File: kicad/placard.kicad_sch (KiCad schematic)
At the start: 0 parts

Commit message: KiCad schematic: 11 main-board sheets and the cartridge, generated
src/scripts/gen_kicad_schematic.py (with kicad_sch_lib.py) writes the
sheets from docs/SCHEMATIC_PLAN.md with every pin's net listed from the
PLD pin lists, basys_top.vhd and the docs.  Decoupling Cn beside each Un,
global labels between sheets, staggered 2 mm labels.  --check compares
KiCad's exported netlist with the script (260 main-board nets, 35 on the
cartridge, no differences).  PDFs in schematics/.  IO.md SD divider refs
now R1003-R1008.

Co-Authored-By: Claude Opus 5.5 (1M context) <noreply@anthropic.com>
Claude-Session: https://claude.ai/code/session_01L9AkLuEg13EebxDmgXsaEp
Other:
- added sheet ALU and registers (alu_regs.kicad_sch)
- added sheet Control (control.kicad_sch)
- added sheet Data bus (data_bus.kicad_sch)
- added sheet Expansion slots (expansion.kicad_sch)
- added sheet Memory and I/O decode (memory.kicad_sch)
- added sheet Power and clock (power.kicad_sch)
- added sheet Program counter and address mux (pc_mux.kicad_sch)
- added sheet Shared port (shared_port.kicad_sch)
- added sheet Video and audio out (video_out.kicad_sch)
- added sheet Video timing (video_timing.kicad_sch)
- note added: "35 chips + U40 regulator (docs/CHIPS.md numbers; U24, U28, U30, U33, U34 are not used)."
- note added: "Decoupling: every chip's 100 nF Cn sits beside Un on its own sheet."
- note added: "HOLD / RUN jumpers"
- note added: "Hierarchy: each box is one sheet; the sheets connect through global labels"
- note added: "J13 USB-C, F201, U40 3.3 V"
- note added: "J9-J12 card-edge slots"
- note added: "Placard main board"
- note added: "Power: +5V, GND, +3V3 (SD card), GNDA (audio, joined to GND on sheet 2)."
- note added: "R601-R608, RN601"
- note added: "The ROM cartridge is its own project: kicad/cartridge/."
- note added: "U1 State, U2 Branch"
- note added: "U11 memory control"
- note added: "U12 I/O decode, U25 map"
- note added: "U13 H, U14 V counters"
- note added: "U15 Sync, U35 audio slots"
- note added: "U16 color decoder, VGA"
- note added: "U17 instruction register"
- note added: "U18 D register"
- note added: "U19 AC, U20 X, U21 Y"
- note added: "U22 pixel buffer, U23 line code"
- note added: "U26, U27 source drivers"
- note added: "U29 line read"
- note added: "U3, U4 program counter"
- note added: "U31, U32 RAM, J8 cartridge"
- note added: "U36 audio DAC, J6"
- note added: "U37 latch, U38 port PLD"
- note added: "U39 rows, J1-J5"
- note added: "U5, U6 ALU"
- note added: "U7-U10 address mux"
- note added: "X1 25.175 MHz, U41 clock gate"
- company: (none) -> Placard computer
- title: Placard -> Placard: Main board
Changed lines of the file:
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@@
 (kicad_sch (version 20230121) (generator eeschema)
   (paper "A3")
-  (title_block
-    (title "Placard")
-    (date "2026-10-19")
-    (rev "0")
-    (comment 1 "PLD computer: see docs/CHIPS.md for parts and U-numbers")
-  )
-  (sheet_instances
-    (path "/" (page "1"))
-  )
+  (title_block (title "Placard: Main board") (date "2026-10-20") (rev "1") (company "Placard computer") (comment 1 "Generated by src/scripts/gen_kicad_schematic.py; plan in docs/SCHEMATIC_PLAN.md") (comment 2 "Chip numbers U1-U41 = docs/CHIPS.md; decoupling Cn goes with Un"))
+  (text "Placard main board" (at 15 22 0) (effects (font (size 6 6) bold) (justify left bottom)))
+  (text "Hierarchy: each box is one sheet; the sheets connect through global labels" (at 15 30 0) (effects (font (size 3 3)) (justify left bottom)))
+  (text "J13 USB-C, F201, U40 3.3 V" (at 23 60 0) (effects (font (size 2.5 2.5)) (justify left bottom)))
+  (text "X1 25.175 MHz, U41 clock gate" (at 23 67 0) (effects (font (size 2.5 2.5)) (justify left bottom)))
+  (text "HOLD / RUN jumpers" (at 23 74 0) (effects (font (size 2.5 2.5)) (justify left bottom)))
+  (text "U1 State, U2 Branch" (at 118 60 0) (effects (font (size 2.5 2.5)) (justify left bottom)))
+  (text "U17 instruction register" (at 118 67 0) (effects (font (size 2.5 2.5)) (justify left bottom)))
+  (text "U3, U4 program counter" (at 213 60 0) (effects (font (size 2.5 2.5)) (justify left bottom)))
+  (text "U7-U10 address mux" (at 213 67 0) (effects (font (size 2.5 2.5)) (justify left bottom)))
+  (text "U31, U32 RAM, J8 cartridge" (at 308 60 0) (effects (font (size 2.5 2.5)) (justify left bottom)))
+  (text "U11 memory control" (at 308 67 0) (effects (font (size 2.5 2.5)) (justify left bottom)))
+  (text "U12 I/O decode, U25 map" (at 308 74 0) (effects (font (size 2.5 2.5)) (justify left bottom)))
+  (text "U5, U6 ALU" (at 118 115 0) (effects (font (size 2.5 2.5)) (justify left bottom)))
+  (text "U19 AC, U20 X, U21 Y" (at 118 122 0) (effects (font (size 2.5 2.5)) (justify left bottom)))
+  (text "U18 D register" (at 213 115 0) (effects (font (size 2.5 2.5)) (justify left bottom)))
+  (text "U26, U27 source drivers" (at 213 122 0) (effects (font (size 2.5 2.5)) (justify left bottom)))
+  (text "R601-R608, RN601" (at 213 129 0) (effects (font (size 2.5 2.5)) (justify left bottom)))
+  (text "U13 H, U14 V counters" (at 23 115 0) (effects (font (size 2.5 2.5)) (justify left bottom)))
+  (text "U15 Sync, U35 audio slots" (at 23 122 0) (effects (font (size 2.5 2.5)) (justify left bottom)))
+  (text "U29 line read" (at 23 129 0) (effects (font (size 2.5 2.5)) (justify left bottom)))
+  (text "U22 pixel buffer, U23 line code" (at 23 170 0) (effects (font (size 2.5 2.5)) (justify left bottom)))
+  (text "U16 color decoder, VGA" (at 23 177 0) (effects (font (size 2.5 2.5)) (justify left bottom)))
+  (text "U36 audio DAC, J6" (at 23 184 0) (effects (font (size 2.5 2.5)) (justify left bottom)))
+  (text "U37 latch, U38 port PLD" (at 118 170 0) (effects (font (size 2.5 2.5)) (justify left bottom)))
+  (text "U39 rows, J1-J5" (at 118 177 0) (effects (font (size 2.5 2.5)) (justify left bottom)))
+  (text "J9-J12 card-edge slots" (at 308 115 0) (effects (font (size 2.5 2.5)) (justify left bottom)))
+  (text "35 chips + U40 regulator (docs/CHIPS.md numbers; U24, U28, U30, U33, U34 are not used)." (at 20 220 0) (effects (font (size 3 3)) (justify left bottom)))
+  (text "Decoupling: every chip's 100 nF Cn sits beside Un on its own sheet." (at 20 224.8 0) (effects (font (size 3 3)) (justify left bottom)))
+  (text "Power: +5V, GND, +3V3 (SD card), GNDA (audio, joined to GND on sheet 2)." (at 20 229.6 0) (effects (font (size 3 3)) (justify left bottom)))
+  (text "The ROM cartridge is its own project: kicad/cartridge/." (at 20 234.4 0) (effects (font (size 3 3)) (justify left bottom)))
+  (sheet (at 20 50) (size 80 35) (fields_autoplaced) (stroke (width 0.3) (type solid)) (fill (color 255 255 225 1.0000)) (property "Sheetname" "Power and clock" (at 20 49.2 0) (effects (font (size 3 3) bold) (justify left bottom))) (property "Sheetfile" "power.kicad_sch" (at 20 85.8 0) (effects (font (size 2 2)) (justify left top))) (instances (project "placard" (path "/e3450542-4ffc-59d4-a4a7-45636233928a" (page "2")))))
+  (sheet (at 115 50) (size 80 35) (fields_autoplaced) (stroke (width 0.3) (type solid)) (fill (color 255 255 225 1.0000)) (property "Sheetname" "Control" (at 115 49.2 0) (effects (font (size 3 3) bold) (justify left bottom))) (property "Sheetfile" "control.kicad_sch" (at 115 85.8 0) (effects (font (size 2 2)) (justify left top))) (instances (project "placard" (path "/e3450542-4ffc-59d4-a4a7-45636233928a" (page "3")))))
+  (sheet (at 210 50) (size 80 35) (fields_autoplaced) (stroke (width 0.3) (type solid)) (fill (color 255 255 225 1.0000)) (property "Sheetname" "Program counter and address mux" (at 210 49.2 0) (effects (font (size 3 3) bold) (justify left bottom))) (property "Sheetfile" "pc_mux.kicad_sch" (at 210 85.8 0) (effects (font (size 2 2)) (justify left top))) (instances (project "placard" (path "/e3450542-4ffc-59d4-a4a7-45636233928a" (page "4")))))
+  (sheet (at 305 50) (size 95 35) (fields_autoplaced) (stroke (width 0.3) (type solid)) (fill (color 255 255 225 1.0000)) (property "Sheetname" "Memory and I/O decode" (at 305 49.2 0) (effects (font (size 3 3) bold) (justify left bottom))) (property "Sheetfile" "memory.kicad_sch" (at 305 85.8 0) (effects (font (size 2 2)) (justify left top))) (instances (project "placard" (path "/e3450542-4ffc-59d4-a4a7-45636233928a" (page "7")))))
+  (sheet (at 115 105) (size 80 35) (fields_autoplaced) (stroke (width 0.3) (type solid)) (fill (color 255 255 225 1.0000)) (property "Sheetname" "ALU and registers" (at 115 104.2 0) (effects (font (size 3 3) bold) (justify left bottom))) (property "Sheetfile" "alu_regs.kicad_sch" (at 115 140.8 0) (effects (font (size 2 2)) (justify left top))) (instances (project "placard" (path "/e3450542-4ffc-59d4-a4a7-45636233928a" (page "5")))))
+  (sheet (at 210 105) (size 80 35) (fields_autoplaced) (stroke (width 0.3) (type solid)) (fill (color 255 255 225 1.0000)) (property "Sheetname" "Data bus" (at 210 104.2 0) (effects (font (size 3 3) bold) (justify left bottom))) (property "Sheetfile" "data_bus.kicad_sch" (at 210 140.8 0) (effects (font (size 2 2)) (justify left top))) (instances (project "placard" (path "/e3450542-4ffc-59d4-a4a7-45636233928a" (page "6")))))
+  (sheet (at 20 105) (size 80 35) (fields_autoplaced) (stroke (width 0.3) (type solid)) (fill (color 255 255 225 1.0000)) (property "Sheetname" "Video timing" (at 20 104.2 0) (effects (font (size 3 3) bold) (justify left bottom))) (property "Sheetfile" "video_timing.kicad_sch" (at 20 140.8 0) (effects (font (size 2 2)) (justify left top))) (instances (project "placard" (path "/e3450542-4ffc-59d4-a4a7-45636233928a" (page "8")))))
+  (sheet (at 20 160) (size 80 35) (fields_autoplaced) (stroke (width 0.3) (type solid)) (fill (color 255 255 225 1.0000)) (property "Sheetname" "Video and audio out" (at 20 159.2 0) (effects (font (size 3 3) bold) (justify left bottom))) (property "Sheetfile" "video_out.kicad_sch" (at 20 195.8 0) (effects (font (size 2 2)) (justify left top))) (instances (project "placard" (path "/e3450542-4ffc-59d4-a4a7-45636233928a" (page "9")))))
+  (sheet (at 115 160) (size 80 35) (fields_autoplaced) (stroke (width 0.3) (type solid)) (fill (color 255 255 225 1.0000)) (property "Sheetname" "Shared port" (at 115 159.2 0) (effects (font (size 3 3) bold) (justify left bottom))) (property "Sheetfile" "shared_port.kicad_sch" (at 115 195.8 0) (effects (font (size 2 2)) (justify left top))) (instances (project "placard" (path "/e3450542-4ffc-59d4-a4a7-45636233928a" (page "10")))))
+  (sheet (at 305 105) (size 95 35) (fields_autoplaced) (stroke (width 0.3) (type solid)) (fill (color 255 255 225 1.0000)) (property "Sheetname" "Expansion slots" (at 305 104.2 0) (effects (font (size 3 3) bold) (justify left bottom))) (property "Sheetfile" "expansion.kicad_sch" (at 305 140.8 0) (effects (font (size 2 2)) (justify left top))) (instances (project "placard" (path "/e3450542-4ffc-59d4-a4a7-45636233928a" (page "11")))))
+  (sheet_instances (path "/" (page "1")))
 )

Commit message: Cartridge loader everywhere: FPGA cartridge model, random RAM, nop at x0000
- src/hdl/cartridge.vhd: the ROM cartridge (loader PLD, EEPROMs from
  rom.mem, SRAM written by /SR_WE); basys_top uses it for RUN, STALL_OUT
  and the ROM data, and the IR PLD replaces the instruction F377
- main RAM and cartridge SRAM start random (gen_random_ram.tcl writes
  ram.mem and cart_ram.mem); build, fast and create_project scripts
  updated, new .vhd files are added to an existing project
- rom_boot and the bring-up ROM keep a nop at x0000 for the hand-off;
  menu and bring-up images rebuilt
- schematic: IR PLD as U17, no 74AC32, STALL_IN/STALL_OUT/PC_ENABLE on
  the cartridge connector, cartridge without the 541; PDFs regenerated
- docs: ROM, CHIPS, BRINGUP, EXPANSION, timing, PLD usage, kitting,
  schematic plan, block diagram
- src/sim/tb_top_load.vhd: whole FPGA model from power-up through the
  load and boot

Co-Authored-By: Claude Opus 5.5 (1M context) <noreply@anthropic.com>
Claude-Session: https://claude.ai/code/session_01PNJoPfzmo1tu8EorCrua96
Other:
- note added: "34 chips + U40 regulator (docs/CHIPS.md numbers; U24, U28, U30, U33, U34 are not used)."
- note added: "STALL / RUN jumpers"
- note added: "U17 instruction register PLD"
- note added: "X1 25.175 MHz clock"
- note removed: "35 chips + U40 regulator (docs/CHIPS.md numbers; U24, U28, U30, U33, U34 are not used)."
- note removed: "HOLD / RUN jumpers"
- note removed: "U17 instruction register"
- note removed: "X1 25.175 MHz, U41 clock gate"
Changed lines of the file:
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@@
   (text "Hierarchy: each box is one sheet; the sheets connect through global labels" (at 15 30 0) (effects (font (size 3 3)) (justify left bottom)))
   (text "J13 USB-C, F201, U40 3.3 V" (at 23 60 0) (effects (font (size 2.5 2.5)) (justify left bottom)))
-  (text "X1 25.175 MHz, U41 clock gate" (at 23 67 0) (effects (font (size 2.5 2.5)) (justify left bottom)))
-  (text "HOLD / RUN jumpers" (at 23 74 0) (effects (font (size 2.5 2.5)) (justify left bottom)))
+  (text "X1 25.175 MHz clock" (at 23 67 0) (effects (font (size 2.5 2.5)) (justify left bottom)))
+  (text "STALL / RUN jumpers" (at 23 74 0) (effects (font (size 2.5 2.5)) (justify left bottom)))
   (text "U1 State, U2 Branch" (at 118 60 0) (effects (font (size 2.5 2.5)) (justify left bottom)))
-  (text "U17 instruction register" (at 118 67 0) (effects (font (size 2.5 2.5)) (justify left bottom)))
+  (text "U17 instruction register PLD" (at 118 67 0) (effects (font (size 2.5 2.5)) (justify left bottom)))
   (text "U3, U4 program counter" (at 213 60 0) (effects (font (size 2.5 2.5)) (justify left bottom)))
   (text "U7-U10 address mux" (at 213 67 0) (effects (font (size 2.5 2.5)) (justify left bottom)))
@@
   (text "U39 rows, J1-J5" (at 118 177 0) (effects (font (size 2.5 2.5)) (justify left bottom)))
   (text "J9-J12 card-edge slots" (at 308 115 0) (effects (font (size 2.5 2.5)) (justify left bottom)))
-  (text "35 chips + U40 regulator (docs/CHIPS.md numbers; U24, U28, U30, U33, U34 are not used)." (at 20 220 0) (effects (font (size 3 3)) (justify left bottom)))
+  (text "34 chips + U40 regulator (docs/CHIPS.md numbers; U24, U28, U30, U33, U34 are not used)." (at 20 220 0) (effects (font (size 3 3)) (justify left bottom)))
   (text "Decoupling: every chip's 100 nF Cn sits beside Un on its own sheet." (at 20 224.8 0) (effects (font (size 3 3)) (justify left bottom)))
   (text "Power: +5V, GND, +3V3 (SD card), GNDA (audio, joined to GND on sheet 2)." (at 20 229.6 0) (effects (font (size 3 3)) (justify left bottom)))

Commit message: Number parts from 1 for each kind; US zigzag resistor symbols
Main board R1-R54, RN1-RN2, D1-D5, JP1-JP2, F1, NT1, non-decoupling
capacitors C41-C46 (decaps keep Cn = Un); keyboard keys 1-63 row by row
(SWn, Dn, Rn per key). Resistors use R_US / R_Network08_US. --check now
fails on gaps or hundreds in the numbering. PDFs regenerated.

Co-Authored-By: Claude Opus 5.5 (1M context) <noreply@anthropic.com>
Claude-Session: https://claude.ai/code/session_01L9AkLuEg13EebxDmgXsaEp
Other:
- note added: "J13 USB-C, F1, U40 3.3 V"
- note added: "R5-R12, RN1"
- note removed: "J13 USB-C, F201, U40 3.3 V"
- note removed: "R601-R608, RN601"
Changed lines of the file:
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@@
   (text "Placard main board" (at 15 22 0) (effects (font (size 6 6) bold) (justify left bottom)))
   (text "Hierarchy: each box is one sheet; the sheets connect through global labels" (at 15 30 0) (effects (font (size 3 3)) (justify left bottom)))
-  (text "J13 USB-C, F201, U40 3.3 V" (at 23 60 0) (effects (font (size 2.5 2.5)) (justify left bottom)))
+  (text "J13 USB-C, F1, U40 3.3 V" (at 23 60 0) (effects (font (size 2.5 2.5)) (justify left bottom)))
   (text "X1 25.175 MHz clock" (at 23 67 0) (effects (font (size 2.5 2.5)) (justify left bottom)))
   (text "STALL / RUN jumpers" (at 23 74 0) (effects (font (size 2.5 2.5)) (justify left bottom)))
@@
   (text "U18 D register" (at 213 115 0) (effects (font (size 2.5 2.5)) (justify left bottom)))
   (text "U26, U27 source drivers" (at 213 122 0) (effects (font (size 2.5 2.5)) (justify left bottom)))
-  (text "R601-R608, RN601" (at 213 129 0) (effects (font (size 2.5 2.5)) (justify left bottom)))
+  (text "R5-R12, RN1" (at 213 129 0) (effects (font (size 2.5 2.5)) (justify left bottom)))
   (text "U13 H, U14 V counters" (at 23 115 0) (effects (font (size 2.5 2.5)) (justify left bottom)))
   (text "U15 Sync, U35 audio slots" (at 23 122 0) (effects (font (size 2.5 2.5)) (justify left bottom)))

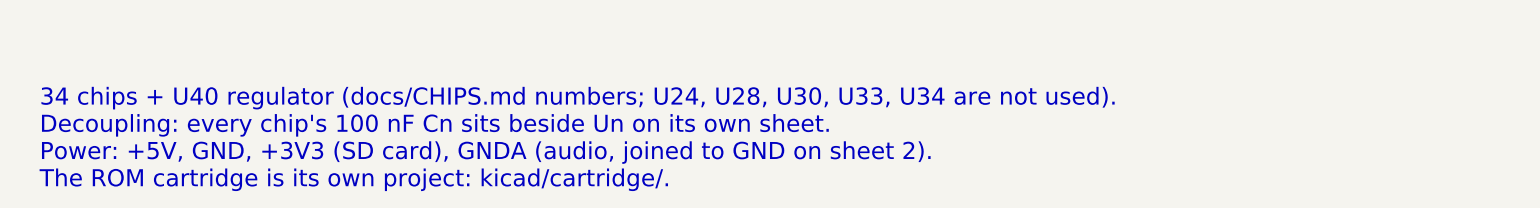
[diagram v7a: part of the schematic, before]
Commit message: Split the ROM cartridge into separate 32K and 64K boards
Two KiCad projects replace the one cartridge with the 32K/64K solder
jumper JP1: kicad/cartridge_64k (U1 loader PLD, U2/U3 EEPROMs, U4/U5
SRAMs) and kicad/cartridge_32k (U1, U2 EEPROM, U3 SRAM, /CE tied to
GND). Each has a placed, netted, unrouted 2-layer board from the new
gen_kicad_cart_pcb.py, with the M3 hole H1 in the gap right above U1 so
it is at the same place (19.5, 25.1 mm) on both boards. New footprint
Card_Edge_87715-9106 (A row on the parts side). Schematic PDFs, BOM and
docs updated; gen_cart_placement.py replaced by the board drawings.

Co-Authored-By: Claude Opus 5.5 (1M context) <noreply@anthropic.com>
Claude-Session: https://claude.ai/code/session_01V16uxpbjEWC9E2eDda9bhu
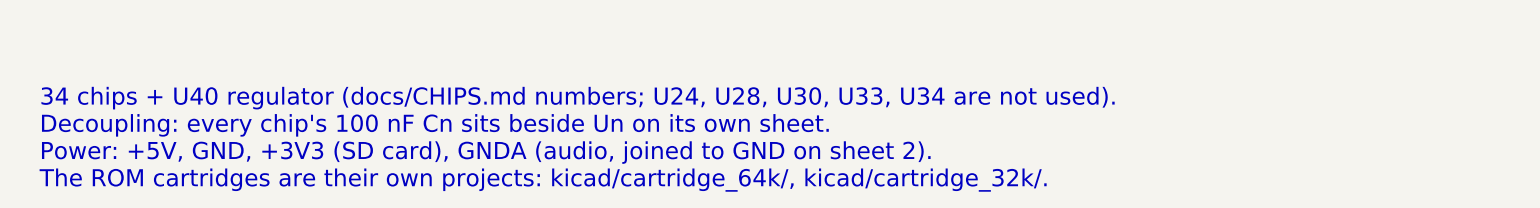
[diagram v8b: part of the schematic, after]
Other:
- note added: "The ROM cartridges are their own projects: kicad/cartridge_64k/, kicad/cartridge_32k/."
- note removed: "The ROM cartridge is its own project: kicad/cartridge/."
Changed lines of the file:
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@@
 (kicad_sch (version 20230121) (generator eeschema)
   (paper "A3")
-  (title_block (title "Placard: Main board") (date "2026-10-23") (rev "1") (company "Placard computer") (comment 1 "Generated by src/scripts/gen_kicad_schematic.py; plan in docs/SCHEMATIC_PLAN.md") (comment 2 "Chip numbers U1-U40 = docs/CHIPS.md; decoupling Cn goes with Un"))
+  (title_block (title "Placard: Main board") (date "2026-10-24") (rev "1") (company "Placard computer") (comment 1 "Generated by src/scripts/gen_kicad_schematic.py; plan in docs/SCHEMATIC_PLAN.md") (comment 2 "Chip numbers U1-U40 = docs/CHIPS.md; decoupling Cn goes with Un"))
   (text "Placard main board" (at 15 22 0) (effects (font (size 6 6) bold) (justify left bottom)))
   (text "Hierarchy: each box is one sheet; the sheets connect through global labels" (at 15 30 0) (effects (font (size 3 3)) (justify left bottom)))
@@
   (text "Decoupling: every chip's 100 nF Cn sits beside Un on its own sheet." (at 20 224.8 0) (effects (font (size 3 3)) (justify left bottom)))
   (text "Power: +5V, GND, +3V3 (SD card), GNDA (audio, joined to GND on sheet 2)." (at 20 229.6 0) (effects (font (size 3 3)) (justify left bottom)))
-  (text "The ROM cartridge is its own project: kicad/cartridge/." (at 20 234.4 0) (effects (font (size 3 3)) (justify left bottom)))
+  (text "The ROM cartridges are their own projects: kicad/cartridge_64k/, kicad/cartridge_32k/." (at 20 234.4 0) (effects (font (size 3 3)) (justify left bottom)))
   (sheet (at 20 50) (size 80 35) (fields_autoplaced) (stroke (width 0.3) (type solid)) (fill (color 255 255 225 1.0000)) (property "Sheetname" "Power and clock" (at 20 49.2 0) (effects (font (size 3 3) bold) (justify left bottom))) (property "Sheetfile" "power.kicad_sch" (at 20 85.8 0) (effects (font (size 2 2)) (justify left top))) (instances (project "placard" (path "/e3450542-4ffc-59d4-a4a7-45636233928a" (page "2")))))
   (sheet (at 115 50) (size 80 35) (fields_autoplaced) (stroke (width 0.3) (type solid)) (fill (color 255 255 225 1.0000)) (property "Sheetname" "Control" (at 115 49.2 0) (effects (font (size 3 3) bold) (justify left bottom))) (property "Sheetfile" "control.kicad_sch" (at 115 85.8 0) (effects (font (size 2 2)) (justify left top))) (instances (project "placard" (path "/e3450542-4ffc-59d4-a4a7-45636233928a" (page "3")))))
